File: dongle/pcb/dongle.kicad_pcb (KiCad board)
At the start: 2 copper layers, 59.7 x 25.2 mm, 31 parts, among them U2 MAX3421EEHJ_T, U3 ESP32-S3-MINI-1, U4 TPS2051BDBVR, U5 NCP167BMX330TBG, X1 SMD-3225_4P12M12PF10PPM

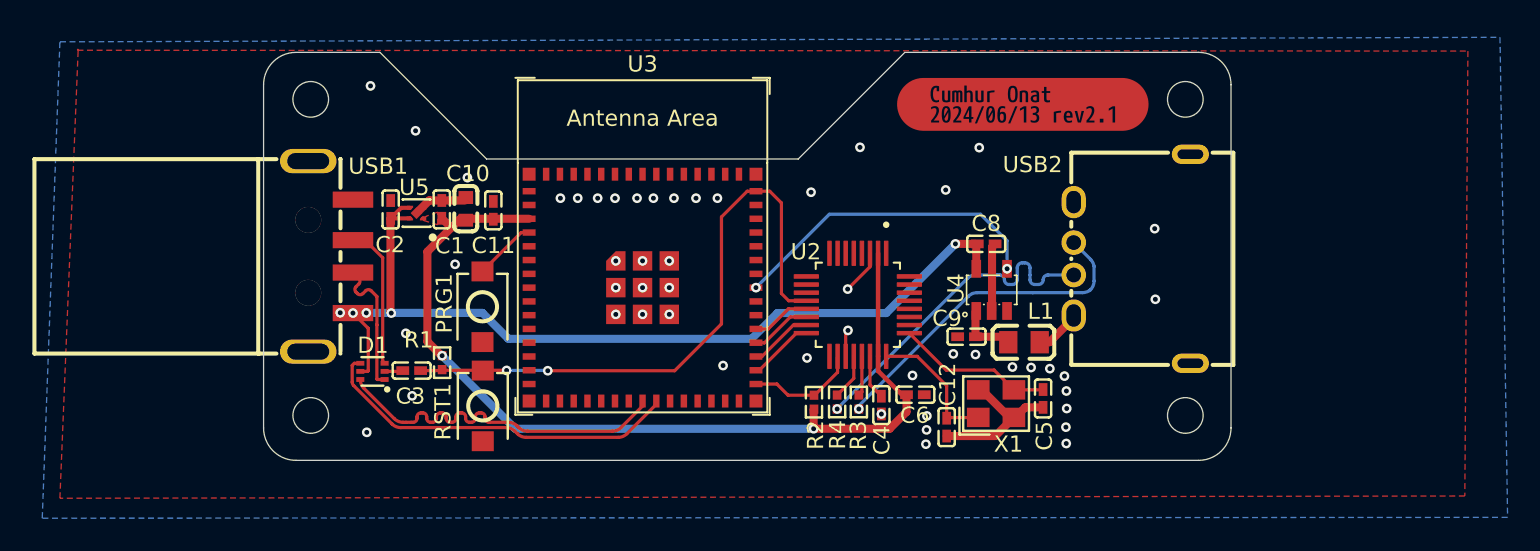
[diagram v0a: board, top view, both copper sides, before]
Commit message: use ch9102f for pc usb
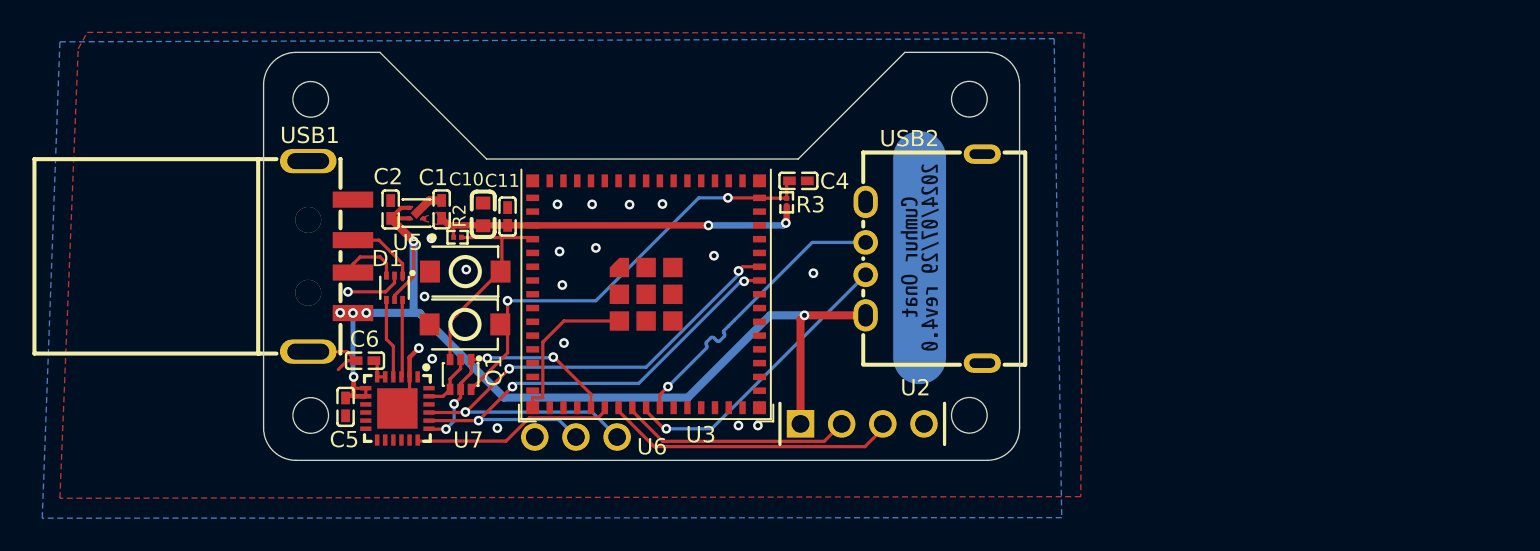
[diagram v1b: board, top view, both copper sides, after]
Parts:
- removed C12: 22pF, dongle:C0402
- removed C3: 1uF, dongle:C0402
- removed C8, C9: 100nF, dongle:C0402
- removed L1: BLM21PG121SN1D, dongle:L0805
- removed PRG1, RST1: TS-1088-AR02016, dongle:SW-SMD_L3.9-W3.0-P4.45
- removed R1: 10K, dongle:R0402
- removed R4: 33, dongle:R0402
- removed U4: TPS2051BDBVR, dongle:SOT-23-5_L3.0-W1.7-P0.95-LS2.8-BR
- removed X1: SMD-3225_4P12M12PF10PPM, dongle:CRYSTAL-SMD_4P-L3.2-W2.5-BL
- removed kibuzzard-666B8349: G***, kibuzzard-666B8349
- added PRG2: TS-1088-AR02016, dongle:SW-SMD_L3.9-W3.0-P4.45, F.Cu at (129.8, 60.9)
- added Q1: MUN5214DW1T1G, dongle:SOT-363_L2.0-W1.3-P0.65-LS2.1-TL, F.Cu at (129.5, 67.2)
- added RST2: TS-1088-AR02016, dongle:SW-SMD_L3.9-W3.0-P4.45, F.Cu at (129.8, 64.2)
- added U6: 2.54-1*3, dongle:HDR-TH_3P-P2.54-V-M-1, F.Cu at (136.6, 71.1)
- added U7: CH9102F, dongle:QFN-24_L4.0-W4.0-P0.50-BL-EP2.5, F.Cu at (125.6, 69.3)
- added kibuzzard-66A861F5: G***, kibuzzard-66A861F5, B.Cu at (157.8, 60.0)
- C5: value 22pF -> 1uF
- C6: value 1uF -> 100nF
- R2: value 10K -> 1k; footprint dongle:R0402 -> dongle:R0201
- R3: value 33 -> 1k; footprint dongle:R0402 -> dongle:R0201
- U2: value MAX3421EEHJ_T -> 2.54-1*4; footprint MAX3421EEHJ_T:QFP50P700X700X120-32N -> dongle:HDR-TH_4P-P2.54-V-M-1
- U3: footprint PCM_Espressif:ESP32-S3-MINI-1 -> dongle:ESP32-S3-MINI-1
- moved C5 43.1 mm to (122.4, 69.2), turned to -90 degrees
- moved C6 34.0 mm to (123.6, 66.4)
- moved R2 24.2 mm to (129.3, 58.8), turned to 180 degrees
- moved C4 14.8 mm to (150.3, 55.3), turned to 0 degrees
- moved H1 13.3 mm to (160.9, 50.3)
- moved H4 13.3 mm to (160.9, 69.8)
- moved R3 13.1 mm to (149.6, 56.6), turned to -90 degrees
- moved USB2 12.8 mm to (158.1, 60.1)
- moved U2 7.36 mm to (154.3, 70.3), turned to 0 degrees
- moved D1 5.34 mm to (125.4, 61.9), turned to 180 degrees
- moved C10 1.12 mm to (130.9, 57.4)
- moved C11 0.96 mm to (132.4, 57.5)
- moved U3 0.47 mm to (140.9, 62.3)
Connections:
- C4 pad 1: GND -> RESET
- C4 pad 2: Net-(U2-VBCOMP) -> GND
- C5 pad 1: GND -> VBUS
- C5 pad 2: Net-(U2-XO) -> GND
- C6 pad 1: 3V3 -> GND
- C6 pad 2: GND -> Net-(U7-V3)
- D1 pad 1: Net-(USB1-D-) -> PCDIN+
- D1 pad 3: Net-(USB1-D+) -> PCDIN-
- D1 pad 4: PCD+ -> PCD-
- D1 pad 6: PCD- -> PCD+
- R2 pad 1: IRQ -> BOOT
- R3 pad 1: CNCD+ -> RESET
- R3 pad 2: Net-(U2-D+) -> 3V3
- U2 pad 1: unconnected-(U2-GPIN7-Pad1) -> VBUS
- U2 pad 2: 3V3 -> U1RX
- U2 pad 3: GND -> U1TX
- U2 pad 4: unconnected-(U2-GPOUT0-Pad4) -> GND
- U3 pad 19: unconnected-(U3-GPIO15/U0RTS/ADC2_CH4/XTAL_32K_P-Pad19) -> RTS
- U3 pad 20: unconnected-(U3-GPIO16/U0CTS/ADC2_CH5/XTAL_32K_N-Pad20) -> CTS
- U3 pad 21: unconnected-(U3-GPIO17/U1TXD/ADC2_CH6-Pad21) -> U1TX
- U3 pad 22: unconnected-(U3-GPIO18/U1RXD/ADC2_CH7/CLK_OUT3-Pad22) -> U1RX
- U3 pad 23: PCD- -> CNCD-
- U3 pad 24: PCD+ -> CNCD+
- U3 pad 31: IRQ -> unconnected-(U3-SPIIO6/GPIO35/FSPID/SUBSPID-Pad31)
- U3 pad 32: MOSI -> unconnected-(U3-SPIIO7/GPIO36/FSPICLK/SUBSPICLK-Pad32)
- U3 pad 33: MISO -> unconnected-(U3-SPIDQS/GPIO37/FSPIQ/SUBSPIQ-Pad33)
- U3 pad 34: CS -> unconnected-(U3-GPIO38/FSPIWP/SUBSPIWP-Pad34)
- U3 pad 35: SCK -> unconnected-(U3-MTCK/GPIO39/CLK_OUT3/SUBSPICS1-Pad35)
- U3 pad 38: VBUSEN -> unconnected-(U3-MTMS/GPIO42-Pad38)
- U3 pad 39: unconnected-(U3-U0TXD/GPIO43/CLK_OUT1-Pad39) -> U0TX
- U3 pad 40: unconnected-(U3-U0RXD/GPIO44/CLK_OUT2-Pad40) -> U0RX
- USB1 pad 2: Net-(USB1-D-) -> PCDIN-
- USB1 pad 3: Net-(USB1-D+) -> PCDIN+
- USB2 pad 1: CNCVBUS -> VBUS
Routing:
- net U0RX: track 0.00 -> 34.8 mm, vias 0 -> 3
- net 3V3: track 57.5 -> 23.3 mm
- net U0TX: track 0.00 -> 30.5 mm, vias 0 -> 3
- net VBUSEN: track 19.8 -> 0.00 mm, vias 2 -> 0
- net PCD+: track 23.0 -> 4.78 mm
- net U1TX: track 0.00 -> 17.9 mm
- net PCD-: track 22.5 -> 4.92 mm
- net RTS: track 0.00 -> 15.2 mm, vias 0 -> 4
- net U1RX: track 0.00 -> 14.3 mm
- net CTS: track 0.00 -> 12.5 mm
- net RESET: track 38.4 -> 27.5 mm
- net Net-(U2-XO): track 9.70 -> 0.00 mm
- net BOOT: track 3.84 -> 13.3 mm
- net Net-(USB1-D+): track 8.85 -> 0.00 mm
- net Net-(USB1-D-): track 8.67 -> 0.00 mm
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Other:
- board size 59.7 x 25.2 mm -> 46.7 x 25.2 mm
